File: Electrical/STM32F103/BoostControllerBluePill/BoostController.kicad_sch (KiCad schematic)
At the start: 57 parts, among them J7 PROG

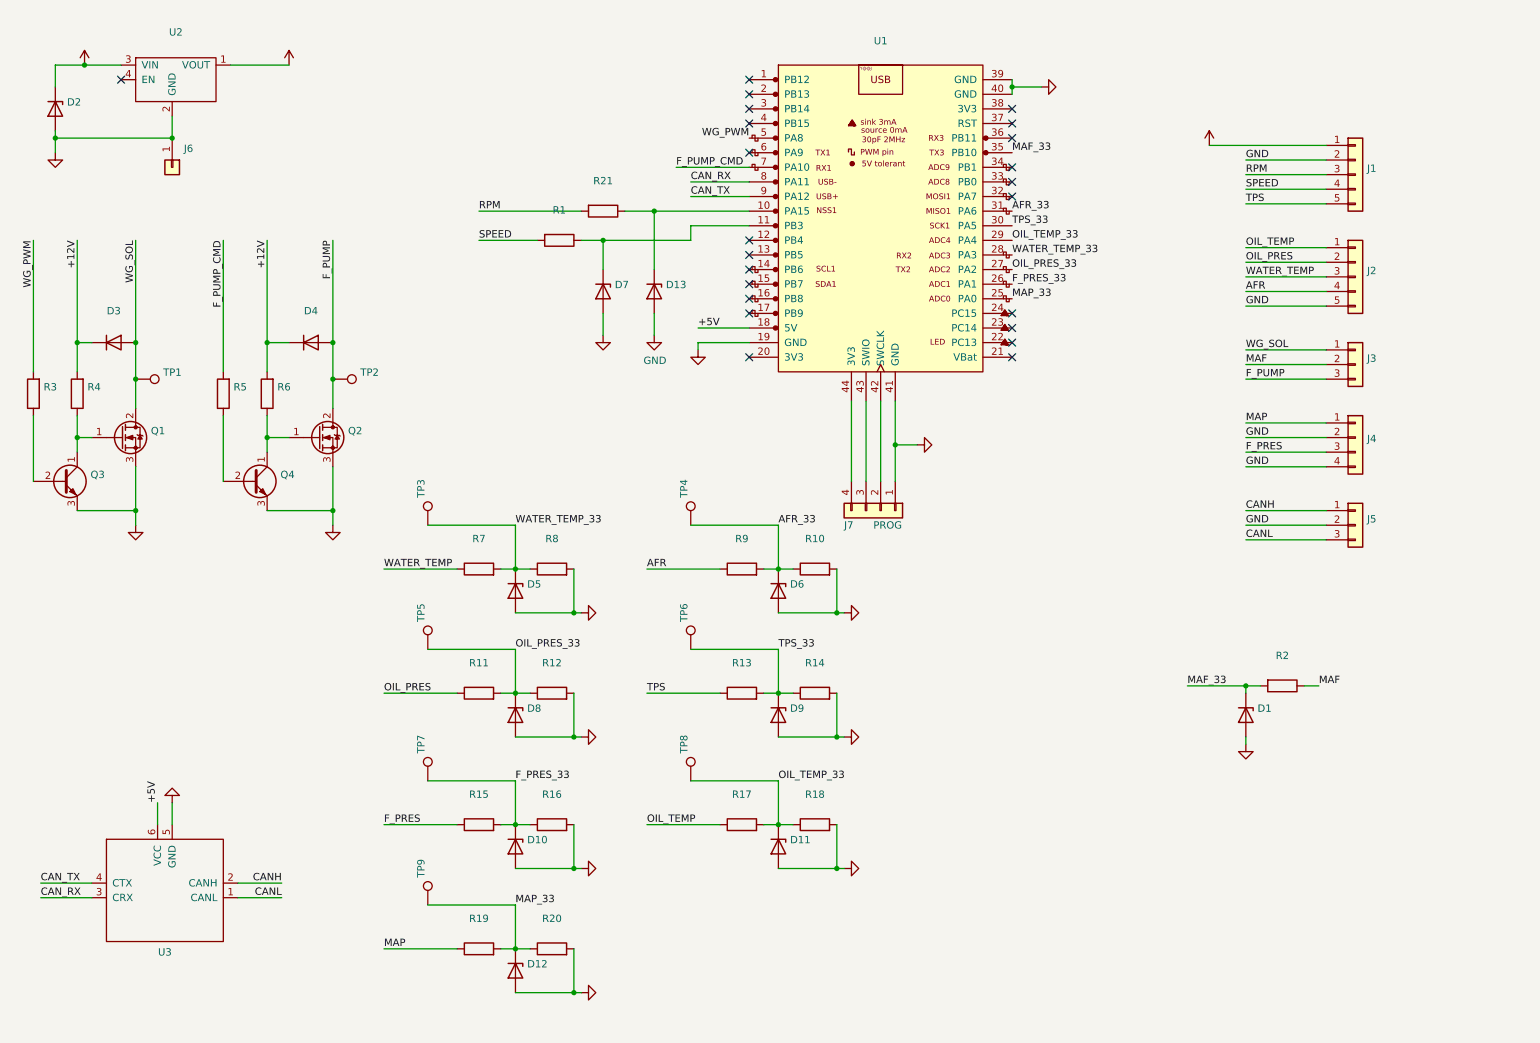
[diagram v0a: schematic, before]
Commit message: Fixed SOT-23 transistors. Added test points. Changed footprint to Kicad6.
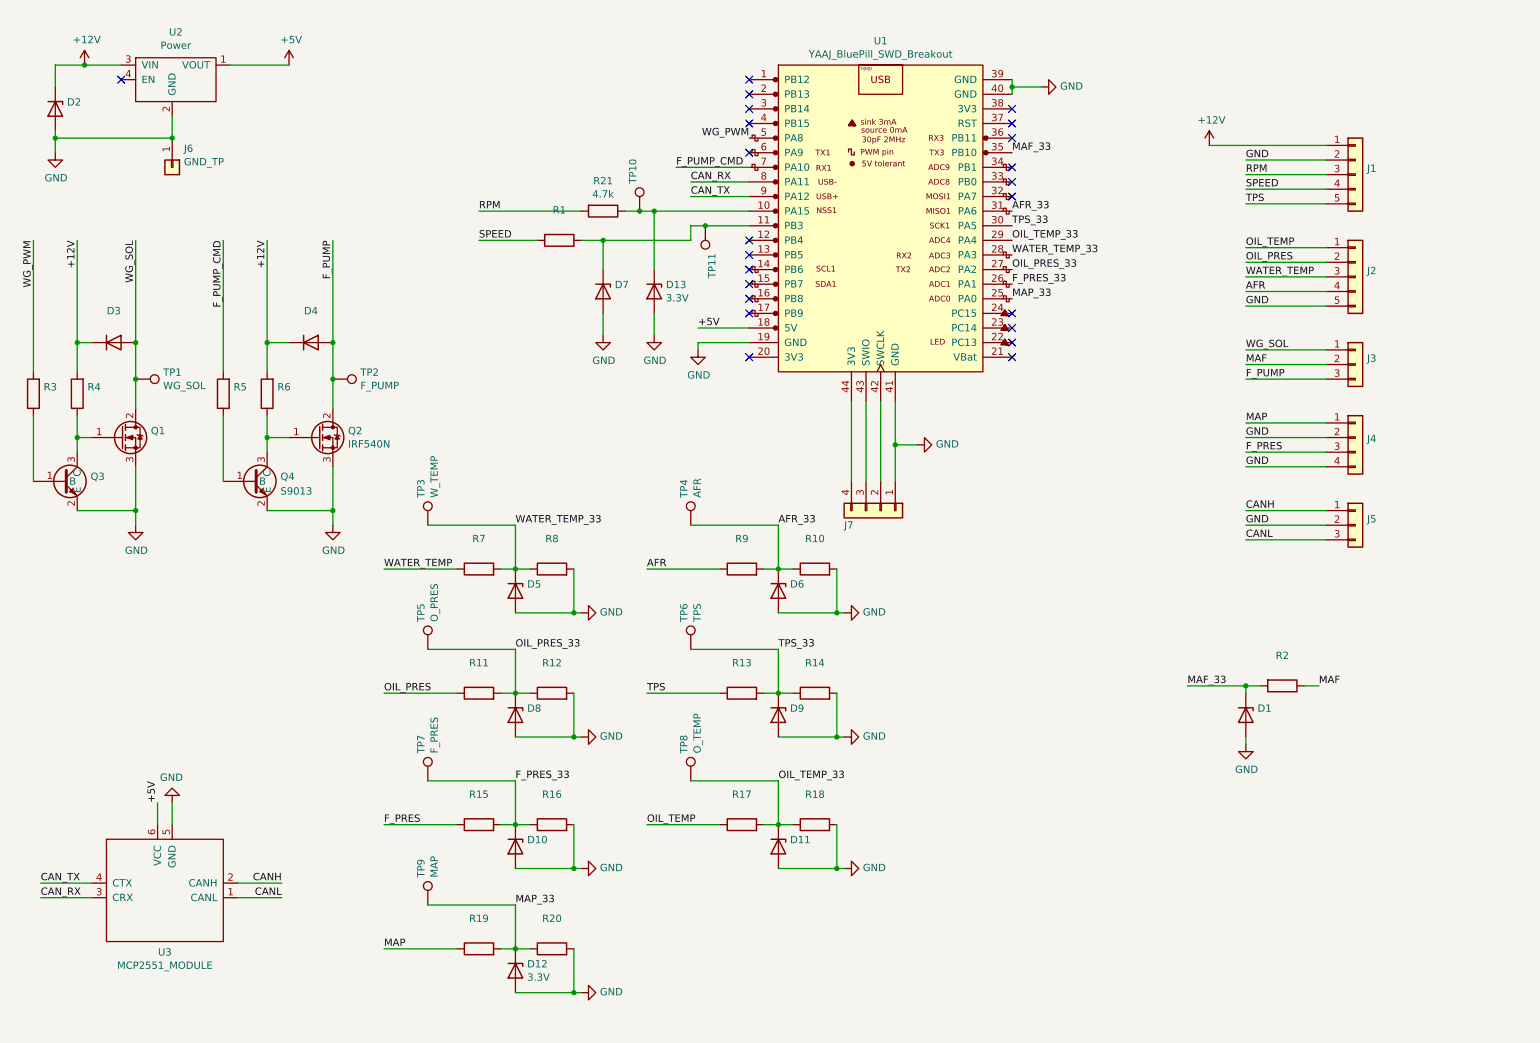
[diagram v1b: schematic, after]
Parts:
- removed Q3, Q4: (no value), symbol Transistor_BJT:BC337
- added Q3: (no value), symbol BoostController-rescue:S9013
- added Q4: S9013, Package_TO_SOT_SMD:SOT-23, symbol BoostController-rescue:S9013
- added TP10, TP11: (no value), symbol Connector:TestPoint
- D12: value (none) -> 3.3V; footprint (none) -> Diodes_SMD:D_MELF_Handsoldering
- D13: value (none) -> 3.3V; footprint (none) -> Diode_SMD:D_MELF_Handsoldering
- J6: value (none) -> GND_TP; footprint (none) -> Pin_Headers:Pin_Header_Straight_1x01_Pitch2.54mm
- J7: value PROG -> (none); footprint Pin_Headers:Pin_Header_Straight_1x04_Pitch2.54mm -> (none)
- Q2: value (none) -> IRF540N; footprint (none) -> Package_TO_SOT_THT:TO-220-3_Vertical
- R21: value (none) -> 4.7k; footprint (none) -> Resistor_SMD:R_1206_3216Metric_Pad1.30x1.75mm_HandSolder
- TP1: value (none) -> WG_SOL; footprint (none) -> Measurement_Points:Measurement_Point_Round-SMD-Pad_Big
- TP2: value (none) -> F_PUMP; footprint (none) -> Measurement_Points:Measurement_Point_Round-SMD-Pad_Big
- TP3: value (none) -> W_TEMP; footprint (none) -> Measurement_Points:Measurement_Point_Round-SMD-Pad_Big
- TP4: value (none) -> AFR; footprint (none) -> Measurement_Points:Measurement_Point_Round-SMD-Pad_Big
- TP5: value (none) -> O_PRES; footprint (none) -> Measurement_Points:Measurement_Point_Round-SMD-Pad_Big
- TP6: value (none) -> TPS; footprint (none) -> Measurement_Points:Measurement_Point_Round-SMD-Pad_Big
- TP7: value (none) -> F_PRES; footprint (none) -> Measurement_Points:Measurement_Point_Round-SMD-Pad_Big
- TP8: value (none) -> O_TEMP; footprint (none) -> Measurement_Points:Measurement_Point_Round-SMD-Pad_Big
- TP9: value (none) -> MAP; footprint (none) -> Measurement_Points:Measurement_Point_Round-SMD-Pad_Big
- U1: value (none) -> YAAJ_BluePill_SWD_Breakout; footprint (none) -> Footprints_pills:YAAJ_BluePill_SWD_1
- U2: value (none) -> Power; footprint (none) -> Sonix:MICRO-BUCK-POWER-MODULE_FLAT
- U3: value (none) -> MCP2551_MODULE; footprint (none) -> Sonix:MCP2551_MODULE
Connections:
- net GND: now also Q3.2 (E), Q4.2 (E)
- net at D13.1 (K), R21.1, U1.10 (PA15): now also TP10.1
- net at D7.1 (K), R1.1, U1.11 (PB3): now also TP11.1
- net at Q1.1 (G), R4.1: now also Q3.3 (C)
- net at Q2.1 (G), R6.1: now also Q4.3 (C)
- net at R3.1: now also Q3.1 (B)
- net at R5.1: now also Q4.1 (B)
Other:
- company: (none) -> Sonix Lab

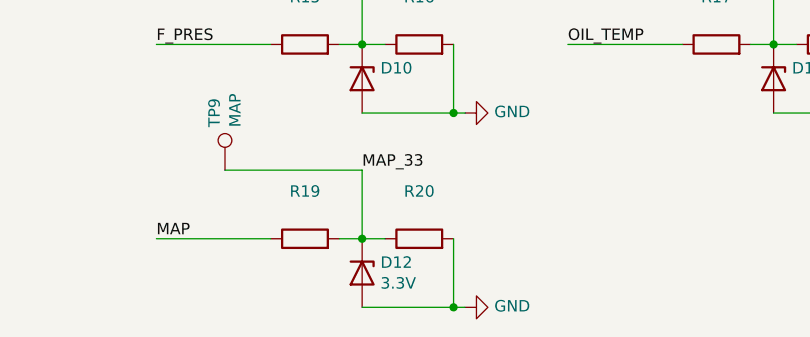
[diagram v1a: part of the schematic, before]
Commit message: Fixed D12 footprint
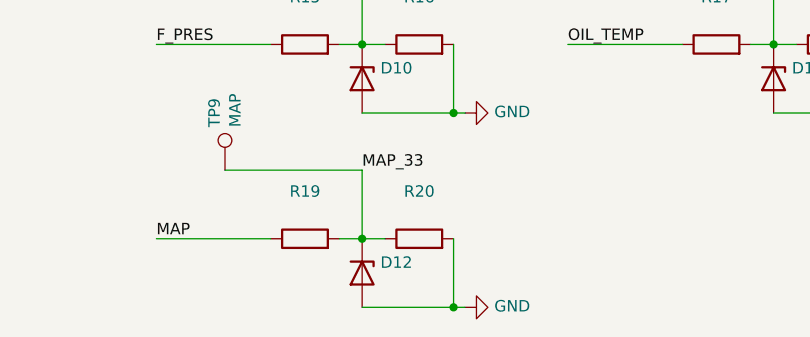
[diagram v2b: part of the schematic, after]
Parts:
- D12: value 3.3V -> (none); footprint Diodes_SMD:D_MELF_Handsoldering -> (none)
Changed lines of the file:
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@@
       (effects (font (size 1.27 1.27)) (justify left))
     )
-    (property "Value" "3.3V" (id 1) (at 109.982 182.753 90)
-      (effects (font (size 1.27 1.27)) (justify left))
-    )
-    (property "Footprint" "Diodes_SMD:D_MELF_Handsoldering" (id 2) (at 107.95 181.61 0)
+    (property "Value" "" (id 1) (at 109.982 182.753 90)
+      (effects (font (size 1.27 1.27)) (justify left))
+    )
+    (property "Footprint" "" (id 2) (at 107.95 181.61 0)
       (effects (font (size 1.27 1.27)) hide)
     )
@@
     )
     (path "/00000000-0000-0000-0000-00006199f232"
-      (reference "D12") (unit 1) (value "3.3V") (footprint "Diodes_SMD:D_MELF_Handsoldering")
+      (reference "D12") (unit 1) (value "3.3V") (footprint "Diode_SMD:D_MELF_Handsoldering")
     )
     (path "/97326434-3dd6-43f2-b2d8-f89ab733a64c"

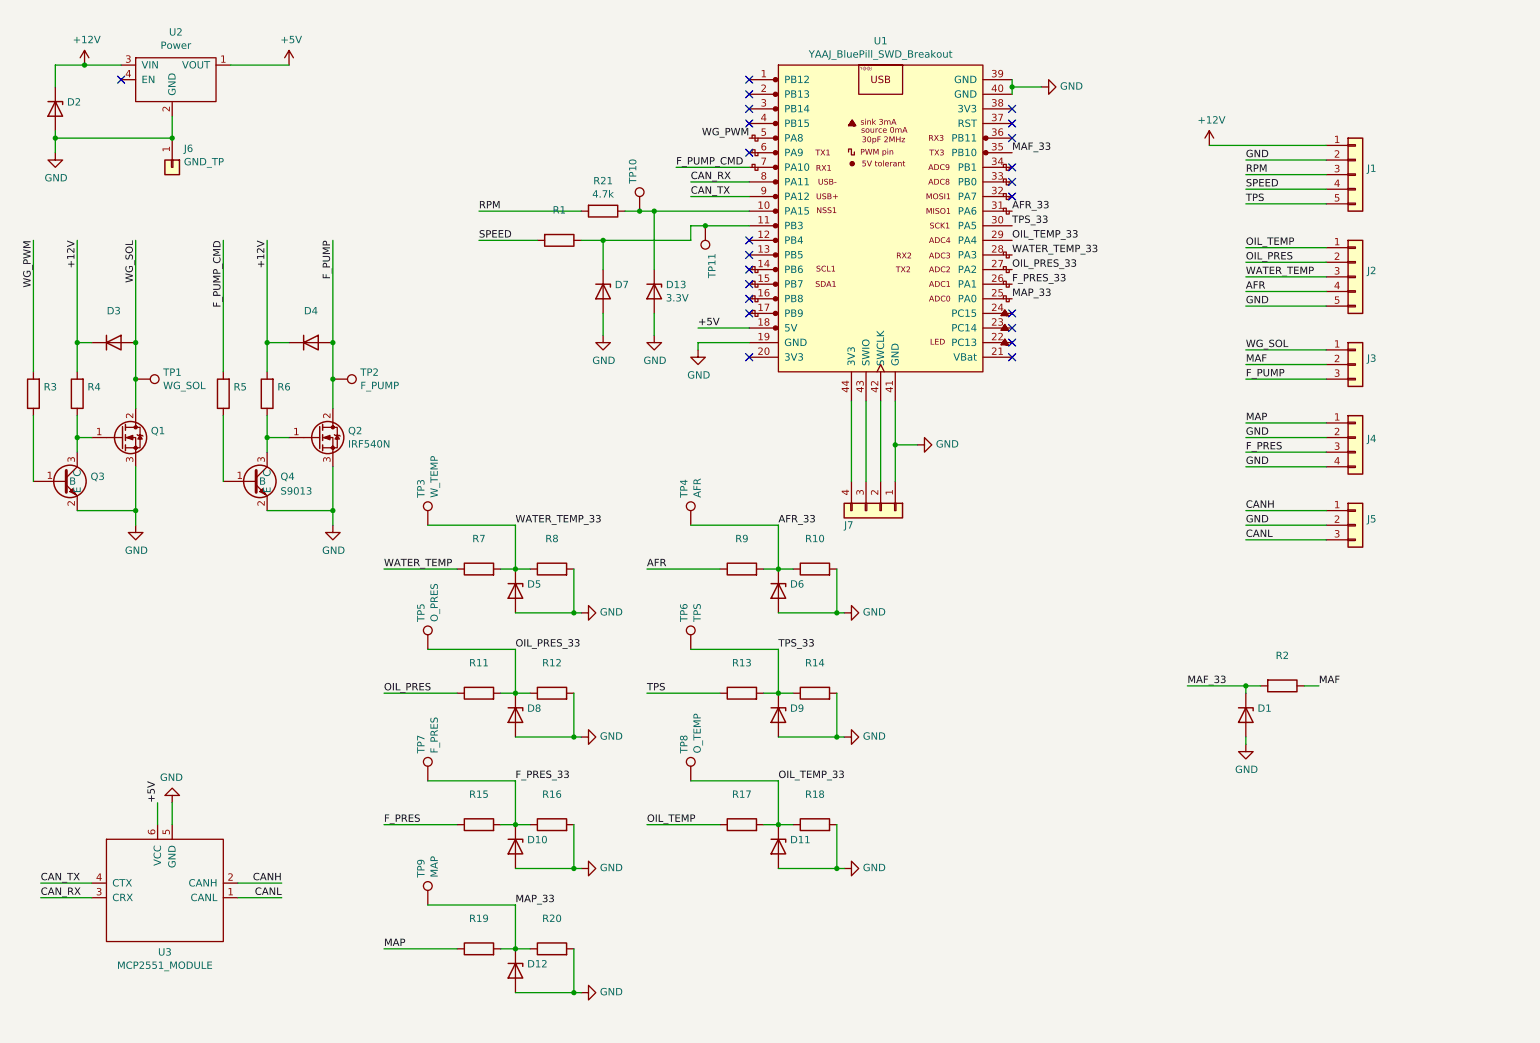
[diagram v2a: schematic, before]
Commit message: Replaced Zener protectio diode (that did not work as expected) with capacitor filter. Replaced MOSFET reference. Clarification on schematic. Changed analog voltage divider resistor values. Added missing test point for MAF input.
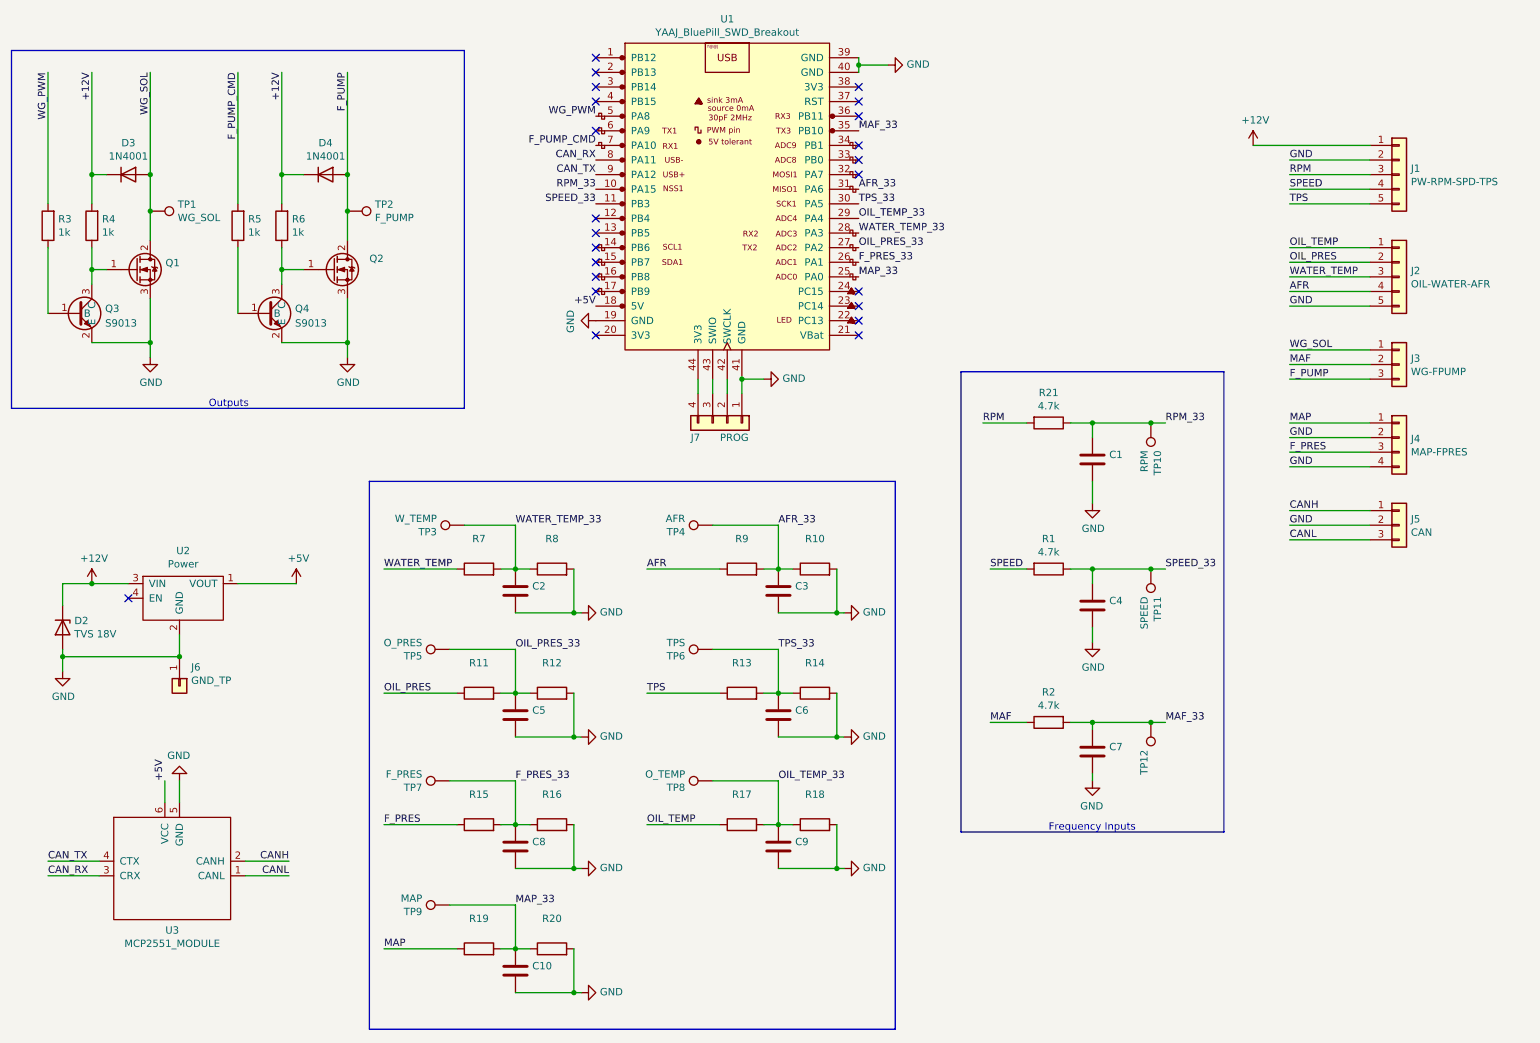
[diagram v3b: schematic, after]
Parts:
- removed D1, D10, D11, D12, D5, D6, D7, D8, D9: (no value), symbol Device:D_Zener
- removed D13: 3.3V, Diode_SMD:D_MELF_Handsoldering, symbol Device:D_Zener
- added C1, C10, C2, C3, C4, C5, C6, C7, C8, C9: (no value), symbol Device:C
- added TP12: (no value), symbol Connector:TestPoint
- D2: value (none) -> TVS 18V; footprint (none) -> Diode_THT:D_DO-41_SOD81_P5.08mm_Vertical_AnodeUp
- D3, D4: value (none) -> 1N4001; footprint (none) -> Diode_THT:D_DO-41_SOD81_P2.54mm_Vertical_AnodeUp
- J1: value (none) -> PW-RPM-SPD-TPS; footprint (none) -> Connector_JST:JST_XH_S5B-XH-A-1_1x05_P2.50mm_Horizontal
- J2: value (none) -> OIL-WATER-AFR; footprint (none) -> Connector_JST:JST_XH_S5B-XH-A-1_1x05_P2.50mm_Horizontal
- J3: value (none) -> WG-FPUMP; footprint (none) -> Connector_JST:JST_XH_S3B-XH-A-1_1x03_P2.50mm_Horizontal
- J4: value (none) -> MAP-FPRES; footprint (none) -> Connector_JST:JST_XH_S4B-XH-A-1_1x04_P2.50mm_Horizontal
- J5: value (none) -> CAN; footprint (none) -> Connector_JST:JST_XH_S3B-XH-A-1_1x03_P2.50mm_Horizontal
- J7: value (none) -> PROG; footprint (none) -> Connector_PinHeader_2.54mm:PinHeader_1x04_P2.54mm_Vertical
- Q2: value IRF540N -> (none); footprint Package_TO_SOT_THT:TO-220-3_Vertical -> (none)
- Q3: value (none) -> S9013; footprint (none) -> Package_TO_SOT_SMD:SOT-23
- R1, R2: value (none) -> 4.7k; footprint (none) -> Resistor_SMD:R_1206_3216Metric_Pad1.30x1.75mm_HandSolder
- R3, R4, R5, R6: value (none) -> 1k; footprint (none) -> Resistor_SMD:R_1206_3216Metric_Pad1.30x1.75mm_HandSolder
- TP10: value (none) -> RPM; footprint (none) -> TestPoint:TestPoint_Pad_D3.0mm
- TP11: value (none) -> SPEED; footprint (none) -> TestPoint:TestPoint_Pad_D3.0mm
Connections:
- net AFR_33: now also C3.1
- net F_PRES_33: now also C8.1
- net GND: now also C1.2, C10.2, C2.2, C3.2, C4.2, C5.2, C6.2, C7.2, C8.2, C9.2
- net MAF_33: now also C7.1, TP12.1
- net MAP_33: now also C10.1
- net OIL_PRES_33: now also C5.1
- net OIL_TEMP_33: now also C9.1
- net TPS_33: now also C6.1
- net WATER_TEMP_33: now also C2.1
- net RPM_33: now reaches R21.1, TP10.1, U1.10 (PA15)
- net RPM_33: now also C1.1
- net SPEED_33: now reaches R1.1, TP11.1, U1.11 (PB3)
- net SPEED_33: now also C4.1
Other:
- note added: "Frequency Inputs"
- note added: "Outputs"
- moved on the sheet: D2, D3, D4, J1, J2, J3, J4, J5, J6, J7, Q1, Q2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
